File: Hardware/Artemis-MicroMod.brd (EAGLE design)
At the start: 22 x 22 mm, 37 parts, among them J1 MICROMOD-2222, U1 ARTEMIS_MODULESMD, U2 TSV524, U6 CH340E_MSOP10, Y1 32.768kHz

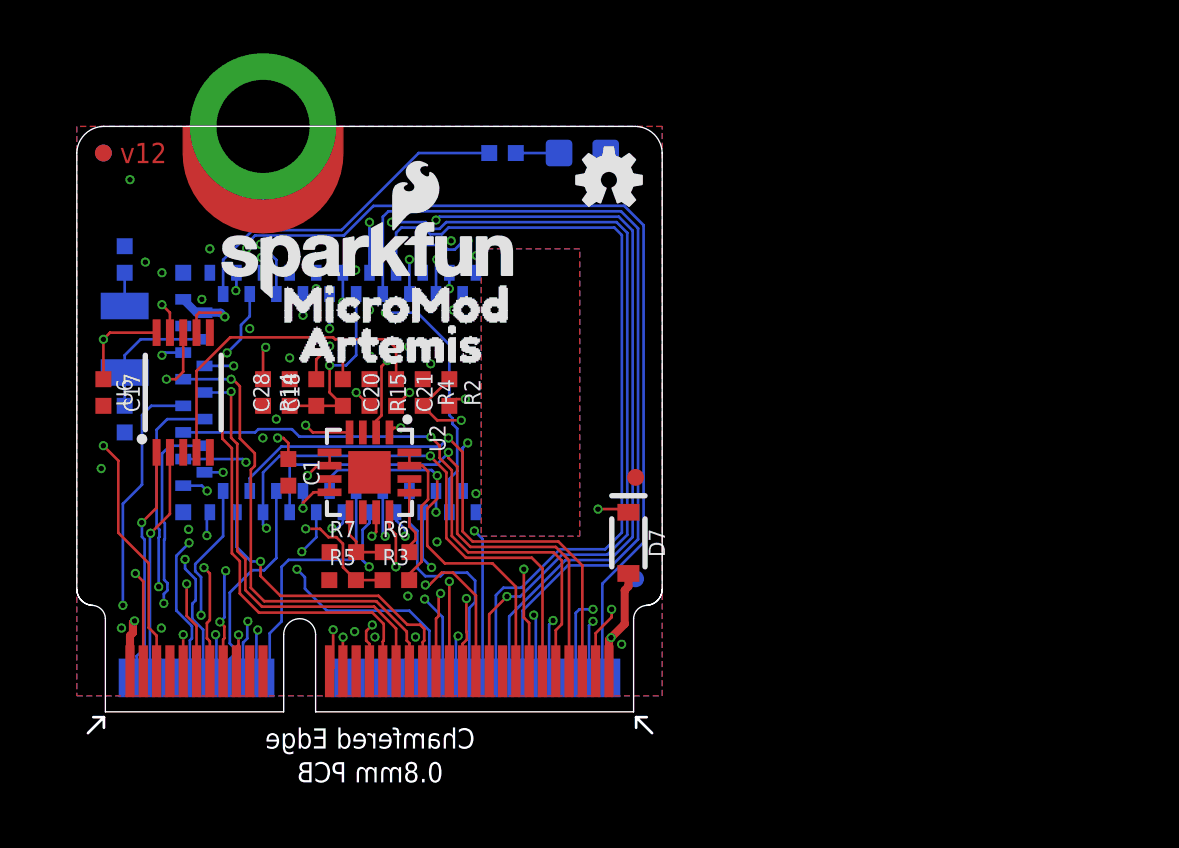
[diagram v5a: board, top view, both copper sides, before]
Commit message: Add MicroMod logo, double route MCLK.
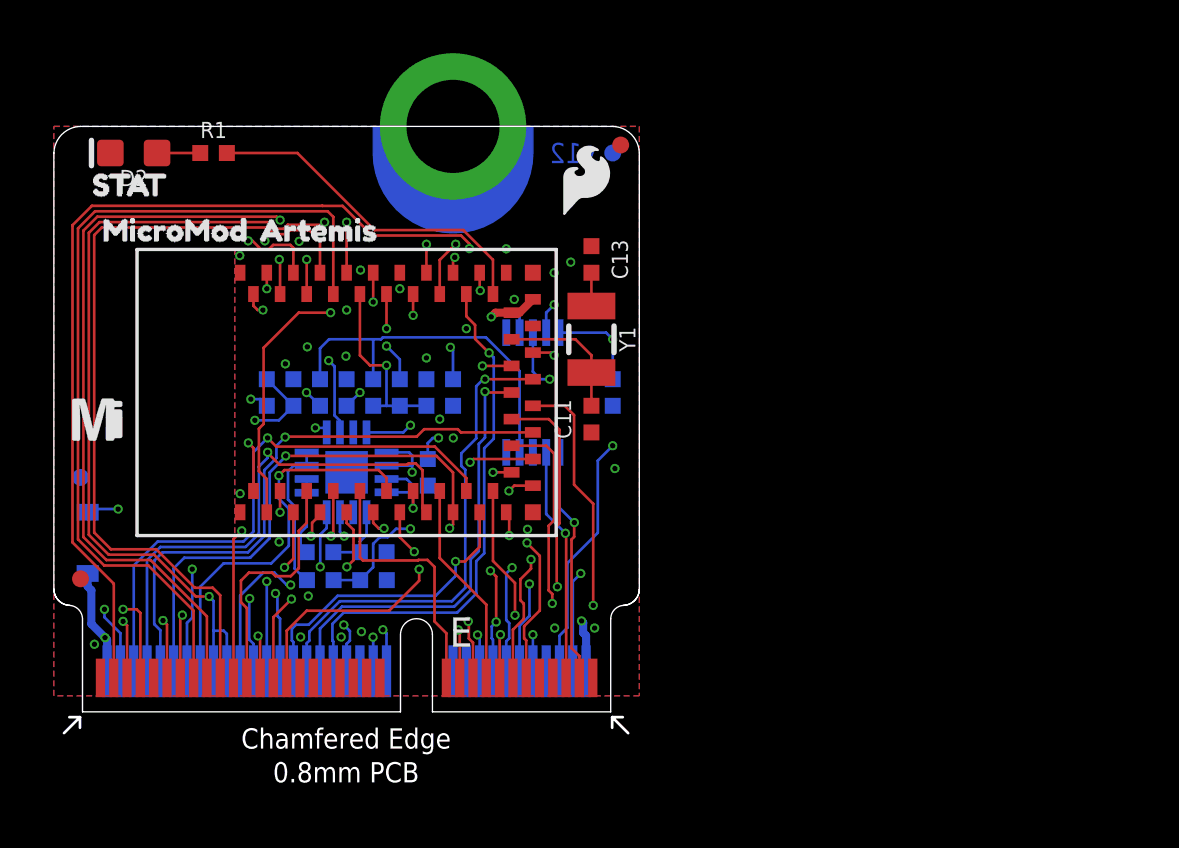
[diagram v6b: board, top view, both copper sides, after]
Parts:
- added LOGO2: SFE_LOGO_FLAME.1_INCH, SparkFun-Aesthetics:SFE_LOGO_FLAME_.1
- added U$4: (no value), SparkFun-Buzzard:STAT_TO_32
- U$1: device SparkFun-Buzzard:STAT_32 -> SparkFun-MicroMod:MICROMOD_MI_LOGO_.35
- moved FRAME1 41.7 mm to (-8.89, -8.89), flipped to the top
- moved LOGO4 26.2 mm to (24.5, 50.8), flipped to the top
- moved U$1 22.1 mm to (1.60, 11.0), flipped to the top
- moved FD1 20.9 mm to (1.00, 5.00), flipped to the top
- moved FD4 20.9 mm to (1.00, 8.81), flipped to the bottom
- moved U$3 20.7 mm to (1.10, 18.1), flipped to the top
- moved D7 20.3 mm to (1.27, 6.35), flipped to the bottom
- moved FD2 19.4 mm to (21.3, 21.3), flipped to the top
- moved C17 19.1 mm to (21.0, 12.0), flipped to the bottom
- moved FD3 19.1 mm to (21.0, 21.0), flipped to the bottom
- moved LOGO3 18.9 mm to (2.00, 20.0), flipped to the bottom
- moved C11 17.5 mm to (20.2, 11.0), flipped to the top
- moved C13 17.5 mm to (20.2, 17.0), flipped to the top
- moved Y1 17.5 mm to (20.2, 14.0), flipped to the top
- moved D2 16.9 mm to (3.00, 21.0), flipped to the top
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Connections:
- removed net SDIO_DATA0: J1.64, U1.~D22, U1.~D6
- removed net SDIO_DATA3: J1.70, U1.~D23
- new net SPI_!CS!1: J1.49, U1.D41
- new net SPI_MISO1: J1.61, U1.~D43
- net CLKOUT: now also J1.58
- net SPI_!CS!: now also J1.70, U1.~D23; no longer J1.49, U1.D41
- net SPI_MISO: now also J1.64, U1.~D22, U1.~D6; no longer J1.61, U1.~D43
- net SPI_MOSI: now also J1.62, U1.D7; no longer J1.59, U1.D38
- net SPI_MOSI1: now also J1.59, U1.D38; no longer J1.62, U1.D7
- net SPI_SCK: now also J1.60, U1.~D5; no longer J1.57, U1.~D42
- net SPI_SCK1: now also J1.57, U1.~D42; no longer J1.60, U1.~D5
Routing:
- net SPI_MISO1: track 0.00 -> 32.5 mm
- net SDIO_DATA0: track 24.4 -> 0.00 mm, vias 3 -> 0
- net SPI_!CS!1: track 0.00 -> 22.9 mm, vias 0 -> 3
- net SDIO_DATA3: track 21.3 -> 0.00 mm, vias 1 -> 0
- net SPI_MOSI1: track 14.3 -> 30.2 mm
- net SPI_MOSI: track 30.2 -> 14.3 mm
- net SPI_SCK: track 30.4 -> 14.7 mm, vias 0 -> 1
- net SPI_SCK1: track 14.7 -> 30.1 mm, vias 1 -> 0
- net SPI_MISO: track 32.5 -> 24.4 mm, vias 0 -> 3
- net CLKOUT: track 31.9 -> 33.6 mm
- net SPI_!CS!: track 22.9 -> 21.3 mm, vias 3 -> 1
- net 3.3V_MAIN: track 27.5 -> 26.3 mm
- net SCALED_ADC1: track 2.52 -> 3.61 mm
- net SCALED_ADC0: track 5.40 -> 6.35 mm
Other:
- outline, holes or cut-outs redrawn
- board text added: "N. Seidle"

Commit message: Add MicroMod logo.
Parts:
- added U$5: (no value), SparkFun-MicroMod:MICROMOD_LOGO_.35
- U$7: device buzzard_labels (1):MICROMOD1 -> SparkFun-MicroMod:MICROMOD_MI_LOGO_.35
- moved U$7 10.7 mm to (20.5, 5.90)
- moved U$6 0.51 mm to (14.3, 13.7)
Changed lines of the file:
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@@
 <element name="U$2" library="buzzard_labels" package="ARTEMIS0" value="" x="7" y="18.1" smashed="yes"/>
 <element name="U$3" library="buzzard_labels" package="MICROMOD1" value="" x="1.1" y="18.1" smashed="yes"/>
-<element name="U$6" library="buzzard_labels (1)" package="ARTEMIS2" value="" x="14.8" y="13.8" smashed="yes" rot="MR0"/>
-<element name="U$7" library="buzzard_labels (1)" package="MICROMOD1" value="" x="15.4" y="15.3" smashed="yes" rot="MR0"/>
+<element name="U$6" library="buzzard_labels (1)" package="ARTEMIS2" value="" x="14.3" y="13.7" smashed="yes" rot="MR0"/>
 <element name="LOGO3" library="SparkFun-Aesthetics" package="OSHW-LOGO-MINI" value="OSHW-LOGOMINI" x="2" y="20" smashed="yes" rot="MR0"/>
 <element name="LOGO4" library="SparkFun-Aesthetics" package="ORDERING_INSTRUCTIONS" value="SPECIAL_INSTRUCTIONS-ORDERING" x="24.54" y="50.8" smashed="yes"/>
@@
 <element name="U$4" library="SparkFun-Buzzard" package="STAT_TO_32" value="" x="0.7" y="19.8" smashed="yes"/>
 <element name="U$1" library="SparkFun-MicroMod" package="MICROMOD_MI_LOGO_.35" value="" x="1.6" y="11" smashed="yes"/>
+<element name="U$5" library="SparkFun-MicroMod" package="MICROMOD_LOGO_.35" value="" x="9.8" y="15.4" smashed="yes" rot="MR0"/>
+<element name="U$7" library="SparkFun-MicroMod" package="MICROMOD_MI_LOGO_.35" value="" x="20.5" y="5.9" smashed="yes" rot="MR0"/>
 </elements>
 <signals>
@@
 <mfgpreviewcolor name="substratecolor" color="0xFF786E46"/>
 </mfgpreviewcolors>
-<errors>
-</errors>
 </board>
 </drawing>

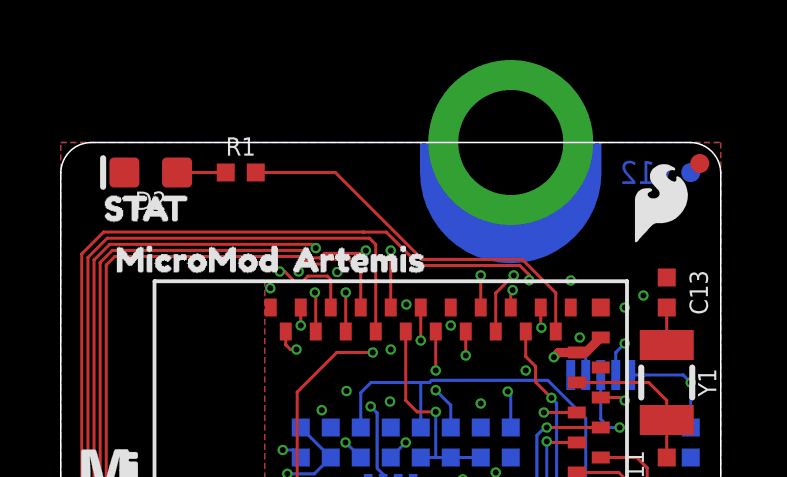
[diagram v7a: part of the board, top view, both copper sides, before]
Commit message: Route from opamp for better AOI. fix DRC error. Add v1.2 panel files.
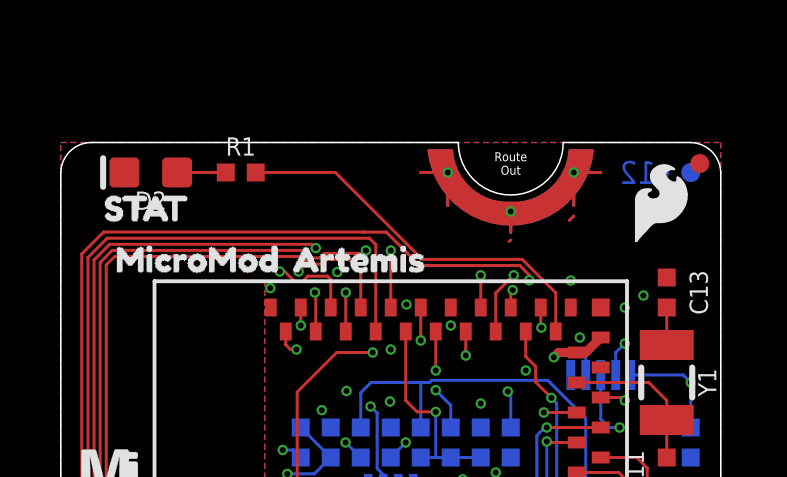
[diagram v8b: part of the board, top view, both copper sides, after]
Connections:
- net GND: now also J1.GND1, J1.GND2, J1.GND3; no longer J1.GND, J1.GND-SM-B
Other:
- outline, holes or cut-outs redrawn
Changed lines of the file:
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@@
 <setting verticaltext="up"/>
 </settings>
-<grid distance="1" unitdist="mm" unit="mm" style="lines" multiple="1" display="yes" altdistance="0.1" altunitdist="mm" altunit="mm"/>
+<grid distance="0.05" unitdist="inch" unit="inch" style="lines" multiple="1" display="yes" altdistance="0.05" altunitdist="mm" altunit="mm"/>
 <layers>
 <layer number="1" name="Top" color="4" fill="1" visible="yes" active="yes"/>
@@
 <layer number="23" name="tOrigins" color="15" fill="1" visible="yes" active="yes"/>
 <layer number="24" name="bOrigins" color="15" fill="1" visible="yes" active="yes"/>
-<layer number="25" name="tNames" color="7" fill="1" visible="no" active="yes"/>
-<layer number="26" name="bNames" color="7" fill="1" visible="no" active="yes"/>
-<layer number="27" name="tValues" color="7" fill="1" visible="no" active="yes"/>
-<layer number="28" name="bValues" color="7" fill="1" visible="no" active="yes"/>
-<layer number="29" name="tStop" color="7" fill="3" visible="no" active="yes"/>
-<layer number="30" name="bStop" color="7" fill="6" visible="no" active="yes"/>
-<layer number="31" name="tCream" color="7" fill="4" visible="no" active="yes"/>
-<layer number="32" name="bCream" color="7" fill="5" visible="no" active="yes"/>
-<layer number="33" name="tFinish" color="6" fill="3" visible="no" active="yes"/>
-<layer number="34" name="bFinish" color="6" fill="6" visible="no" active="yes"/>
-<layer number="35" name="tGlue" color="7" fill="4" visible="no" active="yes"/>
-<layer number="36" name="bGlue" color="7" fill="5" visible="no" active="yes"/>
-<layer number="37" name="tTest" color="7" fill="1" visible="no" active="yes"/>
-<layer number="38" name="bTest" color="7" fill="1" visible="no" active="yes"/>
-<layer number="39" name="tKeepout" color="4" fill="11" visible="no" active="yes"/>
-<layer number="40" name="bKeepout" color="1" fill="11" visible="no" active="yes"/>
-<layer number="41" name="tRestrict" color="4" fill="10" visible="no" active="yes"/>
-<layer number="42" name="bRestrict" color="1" fill="10" visible="no" active="yes"/>
-<layer number="43" name="vRestrict" color="2" fill="10" visible="no" active="yes"/>
-<layer number="44" name="Drills" color="7" fill="1" visible="no" active="yes"/>
+<layer number="25" name="tNames" color="7" fill="1" visible="yes" active="yes"/>
+<layer number="26" name="bNames" color="7" fill="1" visible="yes" active="yes"/>
+<layer number="27" name="tValues" color="7" fill="1" visible="yes" active="yes"/>
+<layer number="28" name="bValues" color="7" fill="1" visible="yes" active="yes"/>
+<layer number="29" name="tStop" color="7" fill="3" visible="yes" active="yes"/>
+<layer number="30" name="bStop" color="7" fill="6" visible="yes" active="yes"/>
+<layer number="31" name="tCream" color="7" fill="4" visible="yes" active="yes"/>
+<layer number="32" name="bCream" color="7" fill="5" visible="yes" active="yes"/>
+<layer number="33" name="tFinish" color="6" fill="3" visible="yes" active="yes"/>
+<layer number="34" name="bFinish" color="6" fill="6" visible="yes" active="yes"/>
+<layer number="35" name="tGlue" color="7" fill="4" visible="yes" active="yes"/>
+<layer number="36" name="bGlue" color="7" fill="5" visible="yes" active="yes"/>
+<layer number="37" name="tTest" color="7" fill="1" visible="yes" active="yes"/>
+<layer number="38" name="bTest" color="7" fill="1" visible="yes" active="yes"/>
+<layer number="39" name="tKeepout" color="4" fill="11" visible="yes" active="yes"/>
+<layer number="40" name="bKeepout" color="1" fill="11" visible="yes" active="yes"/>
+<layer number="41" name="tRestrict" color="4" fill="10" visible="yes" active="yes"/>
+<layer number="42" name="bRestrict" color="1" fill="10" visible="yes" active="yes"/>
+<layer number="43" name="vRestrict" color="2" fill="10" visible="yes" active="yes"/>
+<layer number="44" name="Drills" color="7" fill="1" visible="yes" active="yes"/>
 <layer number="45" name="Holes" color="7" fill="1" visible="yes" active="yes"/>
 <layer number="46" name="Milling" color="3" fill="1" visible="yes" active="yes"/>
-<layer number="47" name="Measures" color="7" fill="1" visible="no" active="yes"/>
-<layer number="48" name="Document" color="7" fill="1" visible="no" active="yes"/>
-<layer number="49" name="Reference" color="7" fill="1" visible="no" active="yes"/>
-<layer number="50" name="dxf" color="7" fill="1" visible="no" active="yes"/>
+<layer number="47" name="Measures" color="7" fill="1" visible="yes" active="yes"/>
+<layer number="48" name="Document" color="7" fill="1" visible="yes" active="yes"/>
+<layer number="49" name="Reference" color="7" fill="1" visible="yes" active="yes"/>
+<layer number="50" name="dxf" color="7" fill="1" visible="yes" active="yes"/>
 <layer number="51" name="tDocu" color="6" fill="1" visible="yes" active="yes"/>
-<layer number="52" name="bDocu" color="7" fill="1" visible="no" active="yes"/>
+<layer number="52" name="bDocu" color="7" fill="1" visible="yes" active="yes"/>
 <layer number="91" name="Nets" color="2" fill="1" visible="no" active="no"/>
 <layer number="92" name="Busses" color="1" fill="1" visible="no" active="no"/>
@@
 <plain>
 <wire x1="0" y1="4.6" x2="0" y2="21" width="0.05" layer="20"/>
-<wire x1="1" y1="22" x2="21" y2="22" width="0.05" layer="20"/>
+<wire x1="1" y1="22" x2="13.25" y2="22" width="0.05" layer="20"/>
+<wire x1="16.75" y1="22" x2="21" y2="22" width="0.05" layer="20"/>
 <wire x1="22" y1="21" x2="22" y2="4.6" width="0.05" layer="20"/>
 <wire x1="21" y1="22" x2="22" y2="21" width="0.05" layer="20" curve="-87.205638"/>
@@
 <text x="19.5" y="21" size="0.762" layer="16" font="vector" ratio="15" rot="SMR0" align="center">v12</text>
 <text x="17.78" y="-8.89" size="1.778" layer="51" font="vector" ratio="15">N. Seidle</text>
+<wire x1="13.25" y1="22" x2="16.75" y2="22" width="0.05" layer="20" curve="180"/>
 </plain>
 <attributes>
@@
 <contactref element="J1" pad="39"/>
 <contactref element="J1" pad="33"/>
-<contactref element="J1" pad="GND-SM-B"/>
+<contactref element="J1" pad="GND2"/>
 <contactref element="J1" pad="36"/>
-<contactref element="J1" pad="GND"/>
+<contactref element="J1" pad="GND1"/>
 <contactref element="J1" pad="7"/>
 <contactref element="J1" pad="1"/>
@@
 <wire x1="10.75" y1="6.76" x2="10.91" y2="6.6" width="0.1016" layer="16"/>
 <via x="10.975" y="13.366" extent="1-16" drill="0.2"/>
+<contactref element="J1" pad="GND3"/>
+<wire x1="15" y1="18.75" x2="14.95" y2="18.7" width="0.1016" layer="1"/>
+<wire x1="17.1" y1="19.55" x2="16.95" y2="19.4" width="0.1016" layer="1"/>
 </signal>
 <signal name="!RESET!">
